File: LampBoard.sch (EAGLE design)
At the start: 25 parts, among them IC1 MEGA8-AI, J1 70543-04, J2 70543-05, T1 BTA25

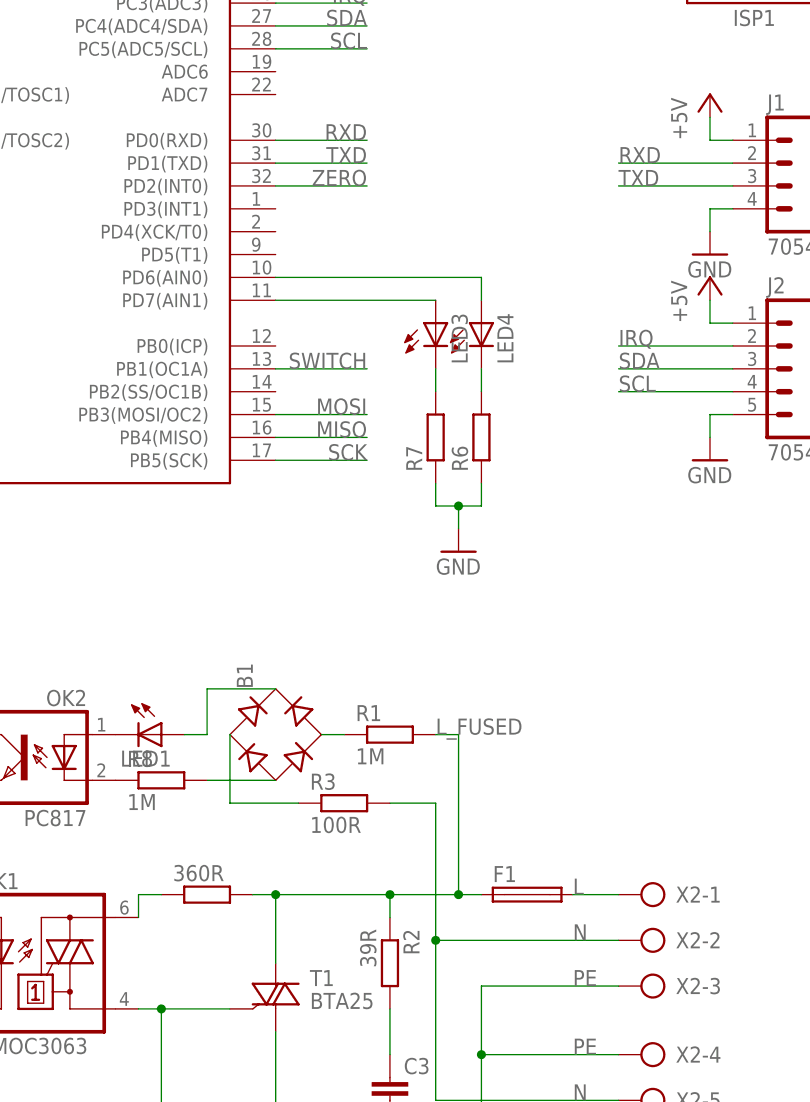
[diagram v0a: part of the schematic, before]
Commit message: AC section routed
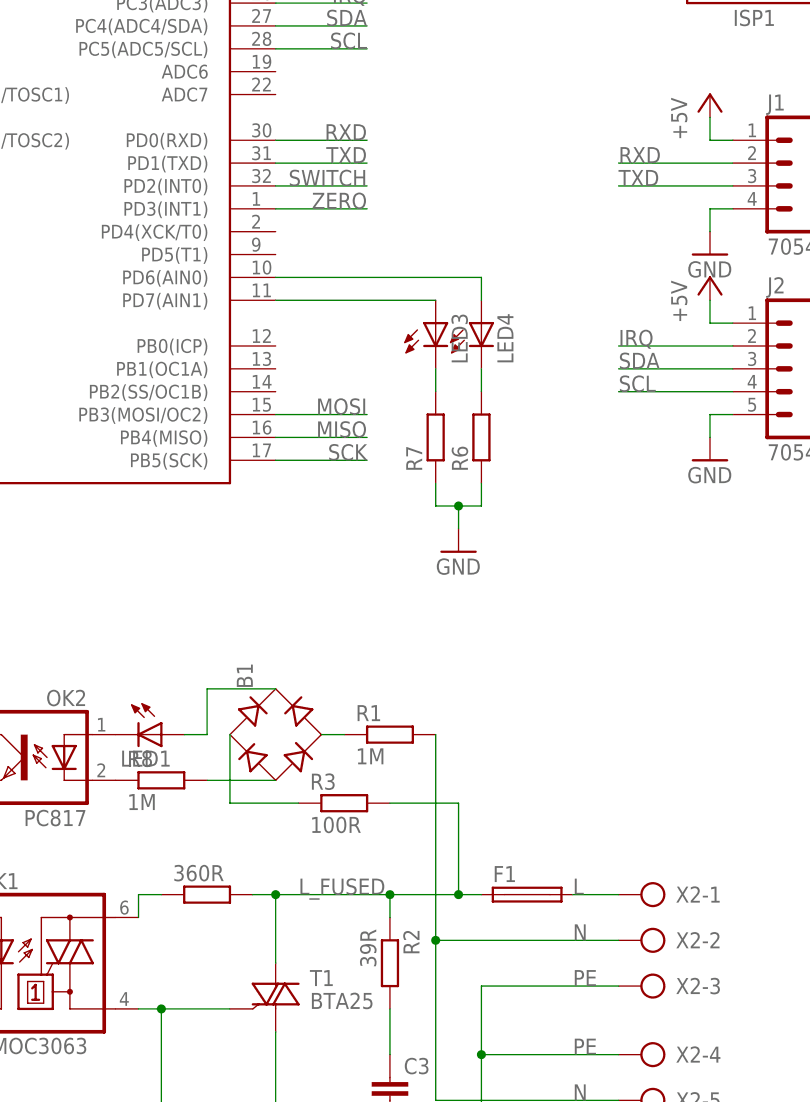
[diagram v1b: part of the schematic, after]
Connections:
- net L_FUSED: now also R3.2; no longer R1.2
- net N: now also R1.2; no longer R3.2
- net SWITCH: now also IC1.PD2(INT0); no longer IC1.PB1(OC1A)
- net ZERO: now also IC1.PD3(INT1); no longer IC1.PD2(INT0)
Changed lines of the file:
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@@
 <pinref part="X2" gate="-2" pin="KL"/>
 <pinref part="X2" gate="-5" pin="KL"/>
-<wire x1="78.74" y1="43.18" x2="78.74" y2="58.42" width="0.1524" layer="91"/>
+<wire x1="78.74" y1="43.18" x2="78.74" y2="66.04" width="0.1524" layer="91"/>
 <junction x="78.74" y="43.18"/>
-<pinref part="R3" gate="G$1" pin="2"/>
-<wire x1="73.66" y1="58.42" x2="78.74" y2="58.42" width="0.1524" layer="91"/>
+<pinref part="R1" gate="G$1" pin="2"/>
 </segment>
 </net>
@@
 <net name="L_FUSED" class="0">
 <segment>
-<label x="78.74" y="66.04" size="1.778" layer="95"/>
-<pinref part="R1" gate="G$1" pin="2"/>
-<wire x1="78.74" y1="66.04" x2="81.28" y2="66.04" width="0.1524" layer="91"/>
+<label x="63.5" y="48.26" size="1.778" layer="95"/>
 <pinref part="T1" gate="G$1" pin="A2"/>
 <wire x1="60.96" y1="48.26" x2="60.96" y2="40.64" width="0.1524" layer="91"/>
@@
 <wire x1="73.66" y1="45.72" x2="73.66" y2="48.26" width="0.1524" layer="91"/>
 <junction x="73.66" y="48.26"/>
-<wire x1="81.28" y1="48.26" x2="81.28" y2="66.04" width="0.1524" layer="91"/>
+<wire x1="81.28" y1="48.26" x2="81.28" y2="58.42" width="0.1524" layer="91"/>
+<pinref part="R3" gate="G$1" pin="2"/>
+<wire x1="73.66" y1="58.42" x2="81.28" y2="58.42" width="0.1524" layer="91"/>
 </segment>
 </net>
@@
 </segment>
 <segment>
-<pinref part="IC1" gate="G$1" pin="PD2(INT0)"/>
-<wire x1="60.96" y1="127" x2="71.12" y2="127" width="0.1524" layer="91"/>
-<label x="71.12" y="127" size="1.778" layer="95" rot="MR0"/>
+<pinref part="IC1" gate="G$1" pin="PD3(INT1)"/>
+<wire x1="60.96" y1="124.46" x2="71.12" y2="124.46" width="0.1524" layer="91"/>
+<label x="71.12" y="124.46" size="1.778" layer="95" rot="MR0"/>
 </segment>
 </net>
@@
 <net name="SWITCH" class="0">
 <segment>
-<pinref part="IC1" gate="G$1" pin="PB1(OC1A)"/>
-<wire x1="60.96" y1="106.68" x2="71.12" y2="106.68" width="0.1524" layer="91"/>
-<label x="71.12" y="106.68" size="1.778" layer="95" rot="MR0"/>
-</segment>
-<segment>
 <label x="-2.54" y="45.72" size="1.778" layer="95"/>
 <pinref part="R5" gate="G$1" pin="1"/>
 <wire x1="7.62" y1="45.72" x2="-5.08" y2="45.72" width="0.1524" layer="91"/>
 </segment>
-</net>
+<segment>
+<pinref part="IC1" gate="G$1" pin="PD2(INT0)"/>
+<wire x1="60.96" y1="127" x2="71.12" y2="127" width="0.1524" layer="91"/>
+<label x="71.12" y="127" size="1.778" layer="95" rot="MR0"/>
+</segment>
+</net>

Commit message: Routing, refacotring
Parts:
- added H1: MOUNT-PAD-ROUND4.5, holes:MOUNT-PAD-ROUND4.5
- added H2, H3: MOUNT-HOLE4.5, holes:MOUNT-HOLE4.5
- LED2, LED3, LED4: device led:LEDCHIPLED_0805 -> led:LED3MM
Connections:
- net PE: now also H1.MOUNT
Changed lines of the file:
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@@
 <part name="P+1" library="supply1" deviceset="+5V" device=""/>
 <part name="R4" library="rcl" deviceset="R-EU_" device="R0805"/>
-<part name="LED3" library="led" deviceset="LED" device="CHIPLED_0805"/>
-<part name="LED4" library="led" deviceset="LED" device="CHIPLED_0805"/>
+<part name="LED3" library="led" deviceset="LED" device="3MM"/>
+<part name="LED4" library="led" deviceset="LED" device="3MM"/>
 <part name="R6" library="rcl" deviceset="R-EU_" device="R0805"/>
 <part name="R7" library="rcl" deviceset="R-EU_" device="R0805"/>
@@
 <part name="B1" library="rectifier" deviceset="B-DIL" device=""/>
 <part name="LED1" library="led" deviceset="LED" device="3MM"/>
-<part name="LED2" library="led" deviceset="LED" device="CHIPLED_0805"/>
+<part name="LED2" library="led" deviceset="LED" device="3MM"/>
 <part name="R8" library="rcl" deviceset="R-EU_" device="0207/10" value="1M"/>
 <part name="ISP1" library="adafruit" deviceset="AVRISP" device="-BOX"/>
@@
 <part name="GND5" library="supply1" deviceset="GND" device=""/>
 <part name="GND6" library="supply1" deviceset="GND" device=""/>
+<part name="H1" library="holes" deviceset="MOUNT-PAD-ROUND" device="4.5"/>
+<part name="H2" library="holes" deviceset="MOUNT-HOLE" device="4.5"/>
+<part name="H3" library="holes" deviceset="MOUNT-HOLE" device="4.5"/>
 </parts>
 <sheets>
@@
 <instance part="R2" gate="G$1" x="73.66" y="40.64" rot="R270"/>
 <instance part="F1" gate="1" x="88.9" y="48.26"/>
-<instance part="PE1" gate="M" x="83.82" y="15.24"/>
+<instance part="PE1" gate="M" x="83.82" y="10.16"/>
 <instance part="X2" gate="-1" x="104.14" y="48.26" rot="R180"/>
 <instance part="X2" gate="-2" x="104.14" y="43.18" rot="R180"/>
@@
 <instance part="GND5" gate="1" x="109.22" y="119.38"/>
 <instance part="GND6" gate="1" x="109.22" y="96.52"/>
+<instance part="H1" gate="G$1" x="88.9" y="15.24"/>
+<instance part="H2" gate="G$1" x="157.48" y="50.8"/>
+<instance part="H3" gate="G$1" x="157.48" y="43.18"/>
 </instances>
 <busses>
@@
 <label x="93.98" y="30.48" size="1.778" layer="95"/>
 <pinref part="X2" gate="-4" pin="KL"/>
-<wire x1="83.82" y1="30.48" x2="83.82" y2="17.78" width="0.1524" layer="91"/>
+<wire x1="83.82" y1="30.48" x2="83.82" y2="15.24" width="0.1524" layer="91"/>
+<wire x1="83.82" y1="15.24" x2="83.82" y2="12.7" width="0.1524" layer="91"/>
 <wire x1="99.06" y1="30.48" x2="83.82" y2="30.48" width="0.1524" layer="91"/>
 <junction x="83.82" y="30.48"/>
+<pinref part="H1" gate="G$1" pin="MOUNT"/>
+<wire x1="86.36" y1="15.24" x2="83.82" y2="15.24" width="0.1524" layer="91"/>
+<junction x="83.82" y="15.24"/>
 </segment>
 </net>

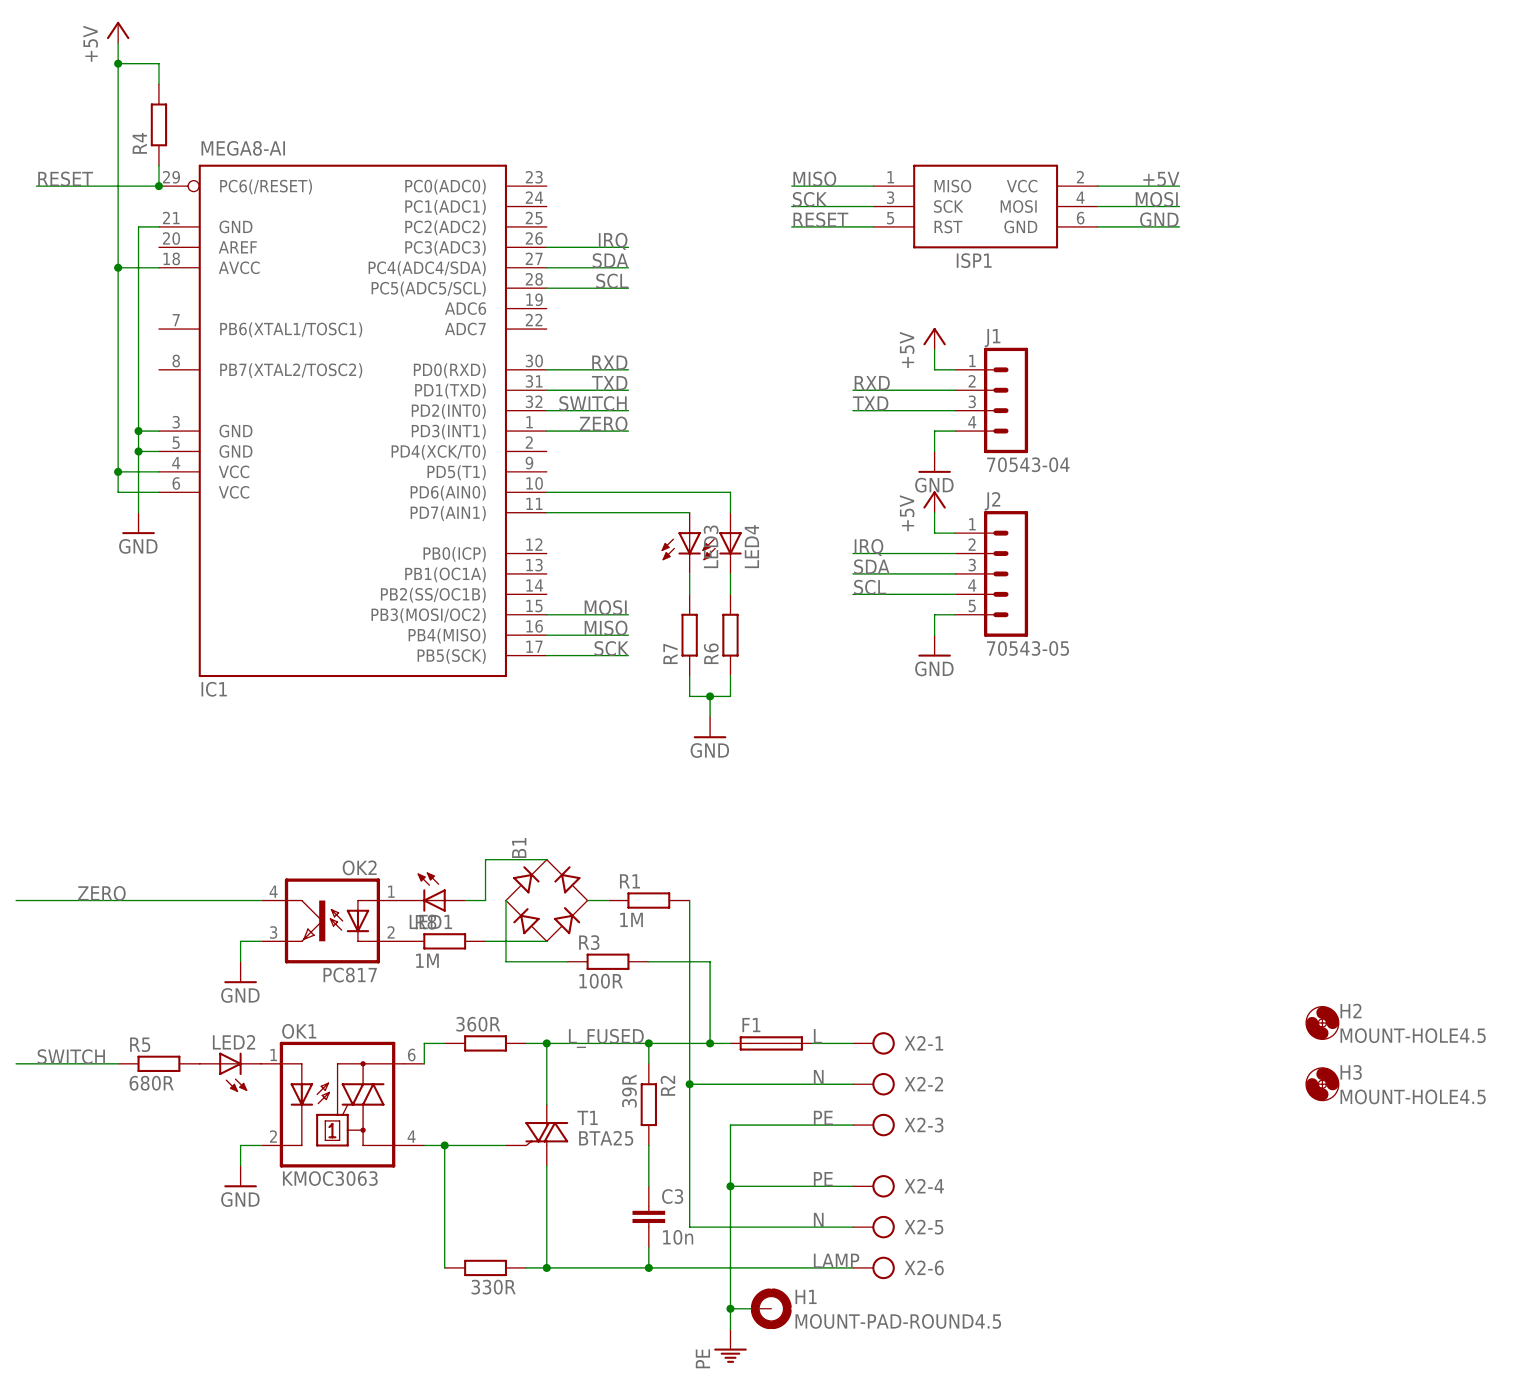
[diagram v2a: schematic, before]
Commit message: Procesor moved away from Power board
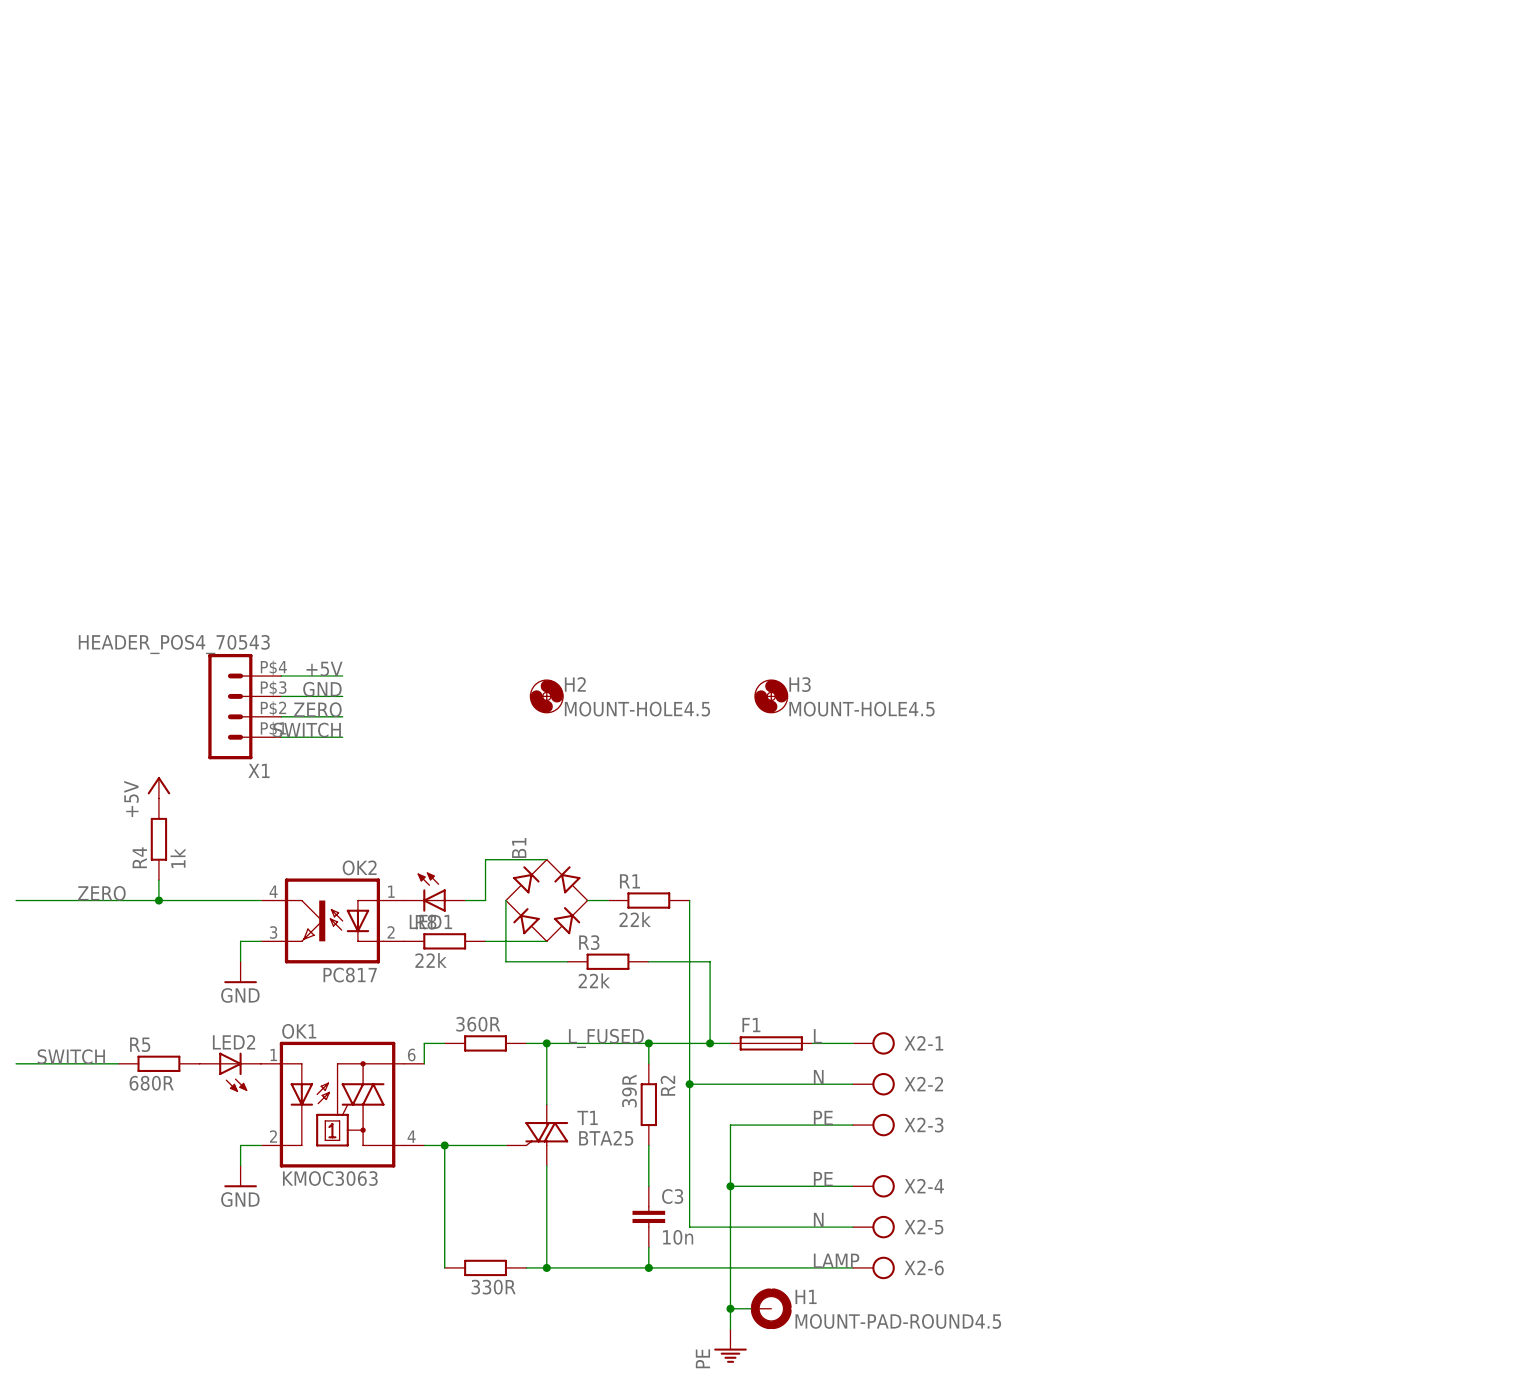
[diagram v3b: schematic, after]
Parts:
- removed IC1: MEGA8-AI, atmel:MEGA8-AI
- removed ISP1: AVRISP-BOX, adafruit:AVRISP-BOX
- removed J1: 70543-04, con-molex-c-grid:70543-04
- removed J2: 70543-05, con-molex-c-grid:70543-05
- removed LED3, LED4: (no value), led:LED3MM
- removed R6, R7: (no value), rcl:R-EU_R0805
- added X1: HEADER_POS4_70543, con-molex-c-grid-sl:HEADER_POS4_70543
- R1, R8: value 1M -> 22k
- R3: value 100R -> 22k
- R4: value (none) -> 1k; device rcl:R-EU_R0805 -> rcl:R-EU_M0805
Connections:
- removed net IRQ: IC1.PC3(ADC3), J2.2
- removed net MISO: IC1.PB4(MISO), ISP1.MISO
- removed net MOSI: IC1.PB3(MOSI/OC2), ISP1.MOSI
- removed net N$10: IC1.PD7(AIN1), LED3.A
- removed net N$13: IC1.PD6(AIN0), LED4.A
- removed net N$14: LED4.C, R6.2
- removed net N$15: LED3.C, R7.2
- removed net RESET: IC1.PC6(/RESET), ISP1.RST, R4.1
- removed net RXD: IC1.PD0(RXD), J1.2
- removed net SCK: IC1.PB5(SCK), ISP1.SCK
- removed net SCL: IC1.PC5(ADC5/SCL), J2.4
- removed net SDA: IC1.PC4(ADC4/SDA), J2.3
- removed net TXD: IC1.PD1(TXD), J1.3
- net +5V: now also X1.4; no longer IC1.AVCC, IC1.VCC@1, IC1.VCC@2, ISP1.VCC, J1.1, J2.1
- net GND: now also X1.3; no longer IC1.GND, IC1.GND@1, IC1.GND@2, ISP1.GND, J1.4, J2.5, R6.1, R7.1
- net SWITCH: now also X1.1; no longer IC1.PD2(INT0)
- net ZERO: now also R4.1, X1.2; no longer IC1.PD3(INT1)
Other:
- moved on the sheet: H2, H3, R4
